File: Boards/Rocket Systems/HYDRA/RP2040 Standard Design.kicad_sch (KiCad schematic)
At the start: 38 parts, among them J10 DX07S016JA1R1500, J7 BM03B-SRSS-TBLFSN, U2 W25Q128JVSIQ TR, U7 ST1L05APU33R

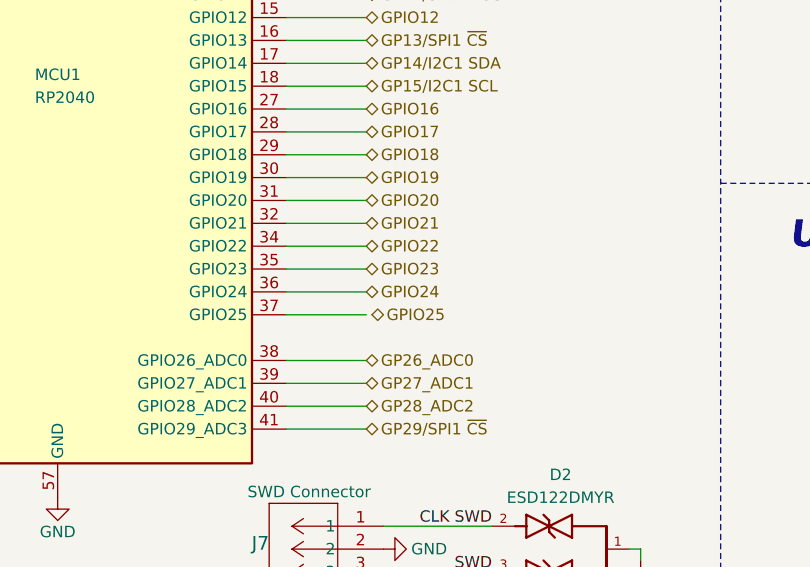
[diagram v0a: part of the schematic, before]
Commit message: updated the ADC routing in schematic
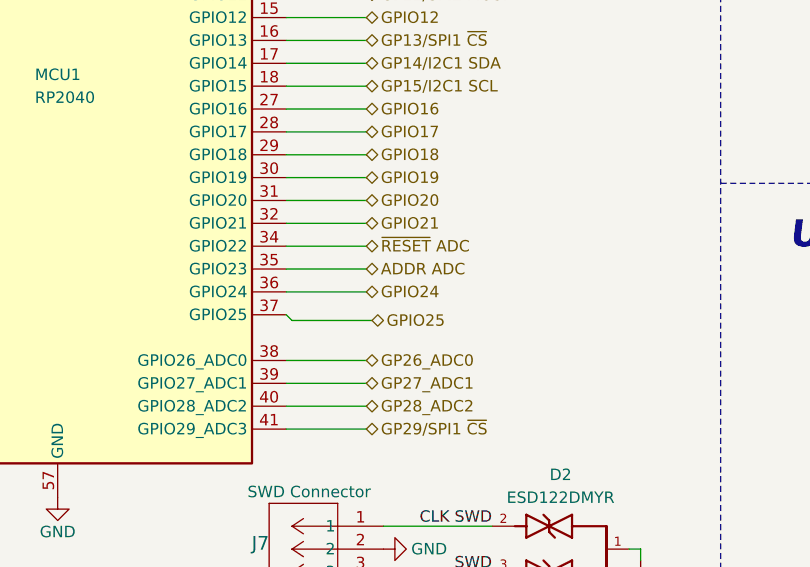
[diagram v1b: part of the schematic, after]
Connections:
- net GPIO25: now also MCU1.37 (GPIO25)
- net GPIO22 renamed ~{RESET} ADC
- net GPIO23 renamed ADDR ADC
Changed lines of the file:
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@@
+	(wire
+		(pts
+			(xy 99.06 124.46) (xy 98.425 123.825)
+		)
+		(stroke
+			(width 0)
+			(type default)
+		)
+	)
 	(wire
 		(pts
@@
 	(wire
 		(pts
-			(xy 98.425 123.825) (xy 107.315 123.825)
+			(xy 99.06 124.46) (xy 107.95 124.46)
 		)
 		(stroke
@@
 		)
 	)
-	(hierarchical_label "GPIO22"
+	(hierarchical_label "~{RESET} ADC"
 		(shape bidirectional)
 		(at 107.315 116.205 0)
@@
 	(hierarchical_label "GPIO25"
 		(shape bidirectional)
-		(at 107.95 123.825 0)
+		(at 107.95 124.46 0)
 		(effects
 			(font
@@
 		)
 	)
-	(hierarchical_label "GPIO23"
+	(hierarchical_label "ADDR ADC"
 		(shape bidirectional)
 		(at 107.315 118.745 0)

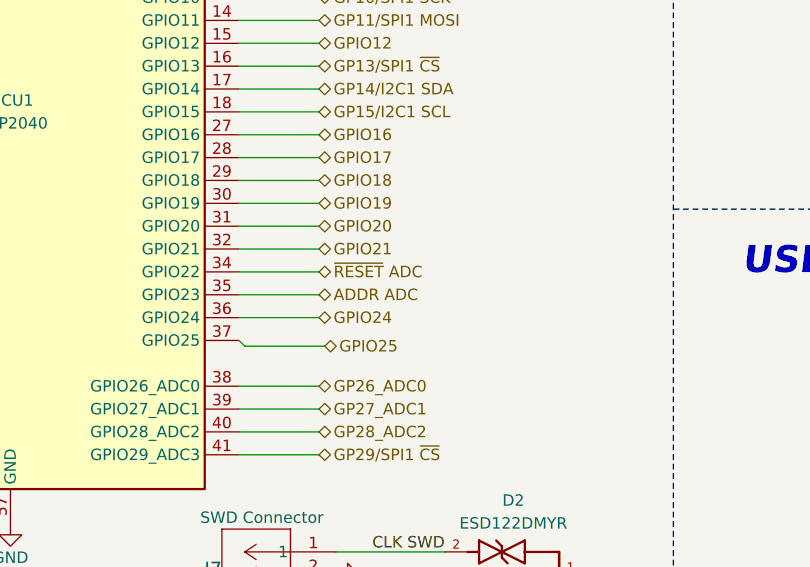
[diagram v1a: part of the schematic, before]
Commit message: major changes on the HYDRA schematic including valve actuation and adc changes
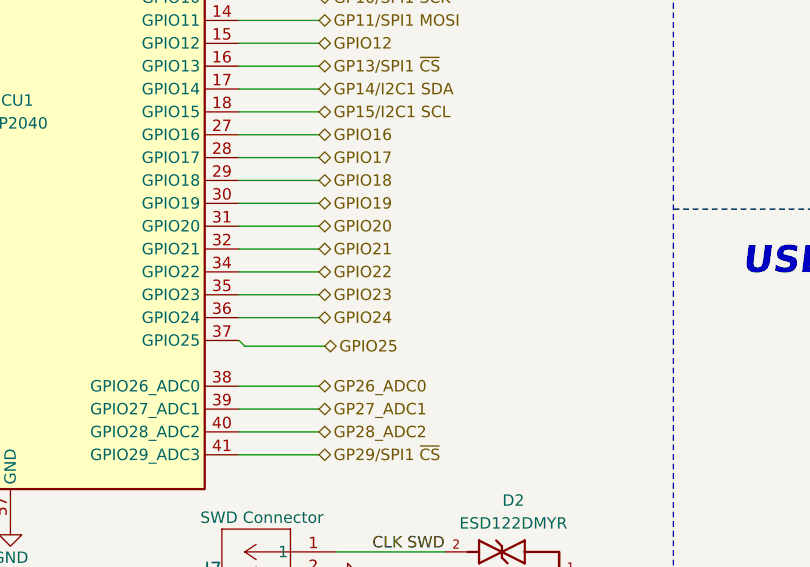
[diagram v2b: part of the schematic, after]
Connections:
- net ADDR ADC renamed GPIO23
- net ~{RESET} ADC renamed GPIO22
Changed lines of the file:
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@@
 		)
 	)
-	(hierarchical_label "~{RESET} ADC"
+	(hierarchical_label "GPIO22"
 		(shape bidirectional)
 		(at 107.315 116.205 0)
@@
 		)
 	)
-	(hierarchical_label "ADDR ADC"
+	(hierarchical_label "GPIO23"
 		(shape bidirectional)
 		(at 107.315 118.745 0)

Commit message: Full HYDRA UPDATE
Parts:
- renumbered C39 to C10, C43 to C11, C31 to C12, C68 to C13, C69 to C14, C34 to C15, C70 to C16, C37 to C17, C71 to C18, C72 to C19, C22 to C3, C20 to C4, C21 to C5, C22 to C6, C31 to C7, C34 to C8, C37 to C9, D2 to D1, D3 to D2, J7 to J1, J10 to J2, JP2 to JP1, JP3 to JP2, R15 to R14, R16 to R15, R17 to R16, R3 to R17, R13 to R18, R20 to R19, R21 to R20, R22 to R21, R23 to R22, R24 to R23, U2 to U3, U7 to U4, XTAL2 to XTAL1
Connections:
- net GPIO2 renamed GP2/PWM1 A

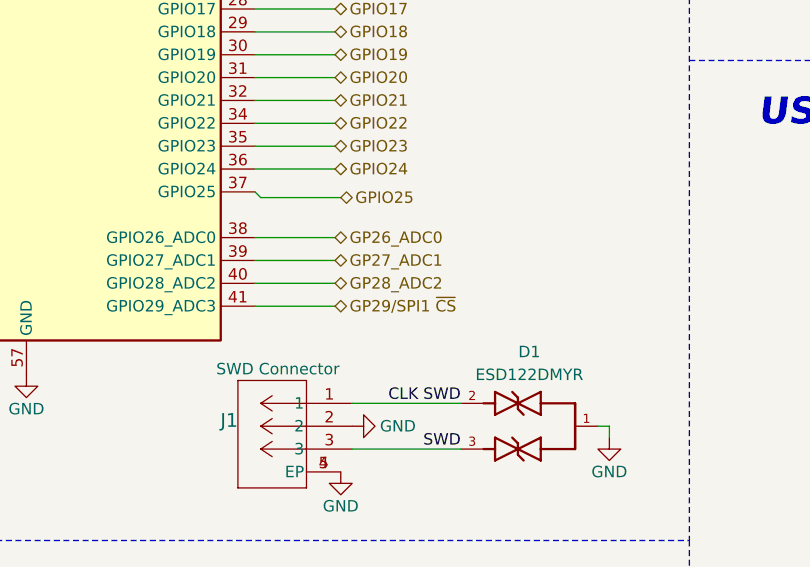
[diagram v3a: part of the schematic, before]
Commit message: HYDRA schematic update, ELYTRA FULL REWORK
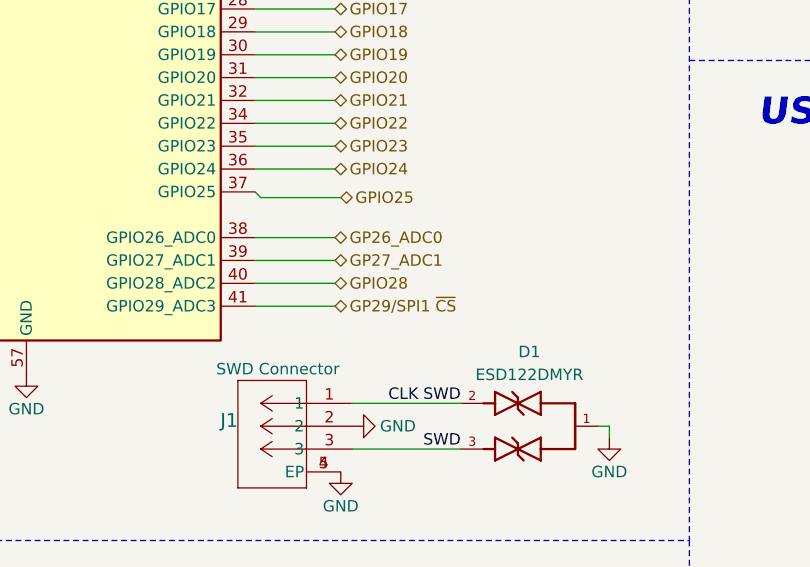
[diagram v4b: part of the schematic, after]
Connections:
- net GP28_ADC2 renamed GPIO28
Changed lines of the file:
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@@
 		)
 	)
-	(hierarchical_label "GP28_ADC2"
+	(hierarchical_label "GPIO28"
 		(shape bidirectional)
 		(at 107.315 133.985 0)

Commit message: HYDRA Update - footprints and schematics
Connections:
- net GPIO28 renamed GP28/PWM6 A
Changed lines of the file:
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@@
+	(wire
+		(pts
+			(xy 98.425 123.825) (xy 107.315 123.825)
+		)
+		(stroke
+			(width 0)
+			(type default)
+		)
+	)
 	(wire
 		(pts
@@
 	(wire
 		(pts
-			(xy 99.06 124.46) (xy 98.425 123.825)
-		)
-		(stroke
-			(width 0)
-			(type default)
-		)
-	)
-	(wire
-		(pts
 			(xy 167.005 136.525) (xy 167.005 134.62)
 		)
@@
 		(pts
 			(xy 215.9 120.65) (xy 215.9 124.46)
-		)
-		(stroke
-			(width 0)
-			(type default)
-		)
-	)
-	(wire
-		(pts
-			(xy 99.06 124.46) (xy 107.95 124.46)
 		)
 		(stroke
@@
 		)
 	)
-	(hierarchical_label "GPIO28"
+	(hierarchical_label "GP28{slash}PWM6 A"
 		(shape bidirectional)
 		(at 107.315 133.985 0)
@@
 	(hierarchical_label "GPIO25"
 		(shape bidirectional)
-		(at 107.95 124.46 0)
-		(effects
-			(font
+		(at 107.315 123.825 0)
+		(effects
+			(font

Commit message: HYDRA placemenent
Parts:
- J1: footprint CONN_BM03B-SRSS-TBLFSN_JST -> SWD_Con:CONN_BM03B-SRSS-TBLFSN_JST
- renumbered C3 to C1, C12 to C10, C13 to C11, C14 to C12, C15 to C13, C16 to C14, C17 to C15, C18 to C16, C19 to C17, C4 to C2, C5 to C3, C6 to C4, C7 to C5, C8 to C6, C9 to C7, C10 to C8, C11 to C9, R14 to R12, R15 to R13, R16 to R14, R17 to R15, R18 to R16, R19 to R17, R20 to R18, R21 to R19, R22 to R20, R23 to R21
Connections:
- net USB_DN: now also D2.3 (IO2), D2.4 (IO3); no longer D2.1 (IO1), D2.6 (IO4)
- net USB_DP: now also D2.1 (IO1), D2.6 (IO4); no longer D2.3 (IO2), D2.4 (IO3)
- net GP28/PWM6 A renamed GPIO28
- net GP2/PWM1 A renamed GPIO2
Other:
- title: RP2040 Standard -> Hydraulic Regulation & Actuation system
